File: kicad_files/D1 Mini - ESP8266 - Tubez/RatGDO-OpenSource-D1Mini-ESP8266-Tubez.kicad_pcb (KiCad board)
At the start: 2 copper layers, 51.8 x 65.8 mm, 27 parts, among them J1 Screw_Terminal_01x03, J2 Conn_01x11, J3 Screw_Terminal_01x02, Q1 2N7002, Q2 AO3400A, Q3 AO3400A, Q4 AO3400A, U1 WeMos_D1_mini, U2 K7805-500R3

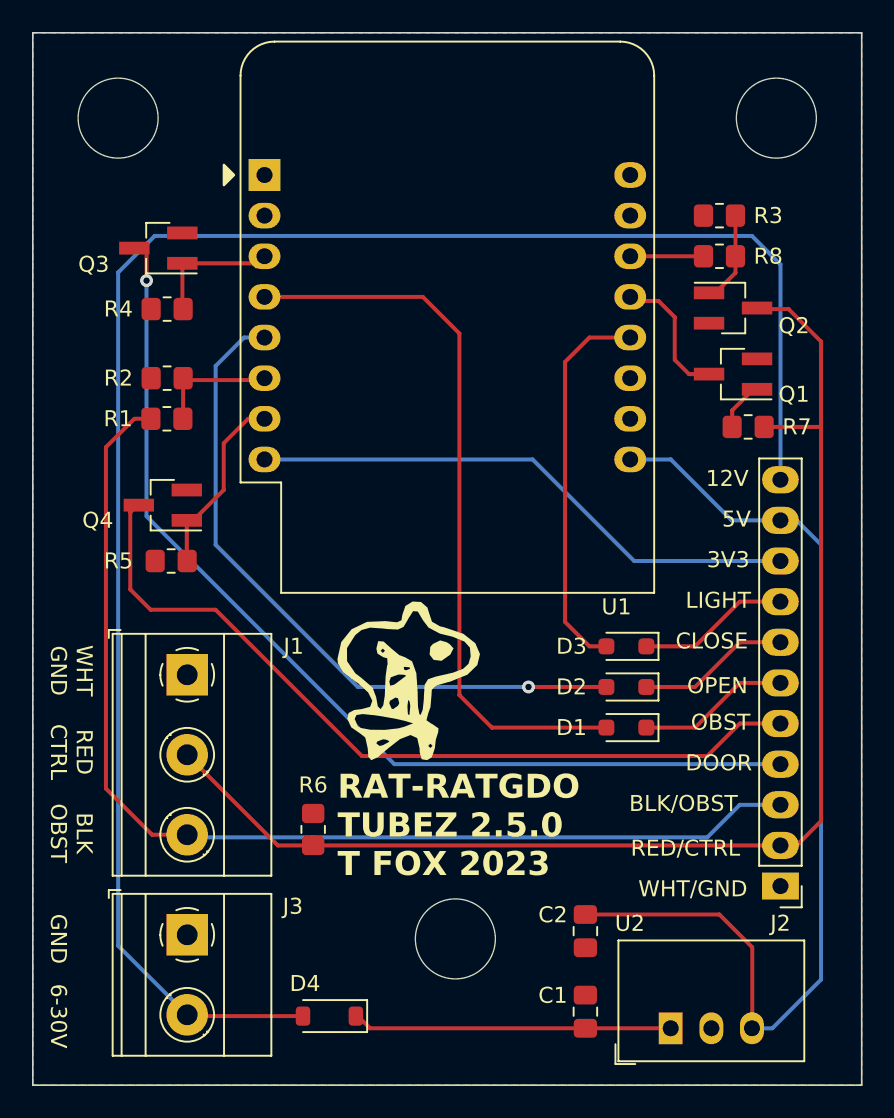
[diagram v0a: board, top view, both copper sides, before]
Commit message: Addition of R7/R6 and R8
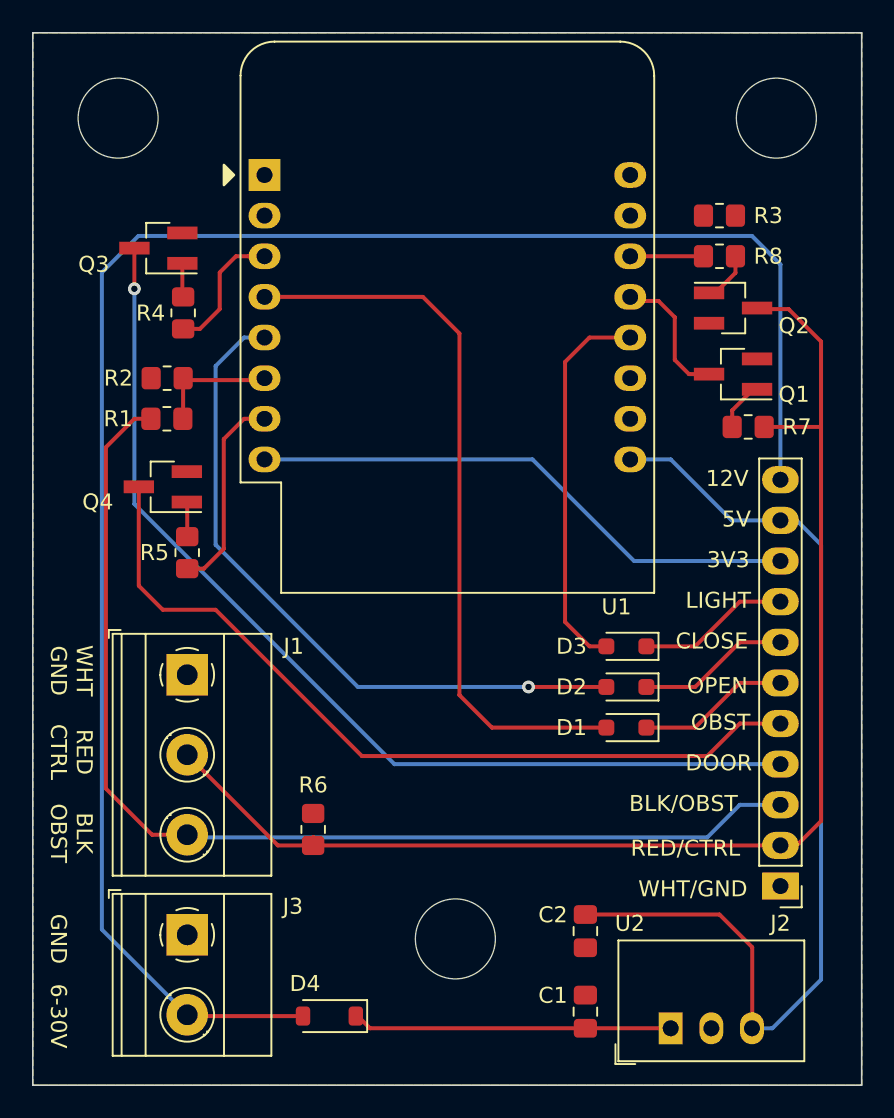
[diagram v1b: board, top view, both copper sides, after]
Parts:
- G***: moved to B.Cu
- moved G*** 3.31 mm to (141.2, 95.8), turned to 180 degrees
- moved Q4 1.15 mm to (123.2, 85.5)
- moved R5 1.13 mm to (124.7, 89.6), turned to 90 degrees
- moved R4 1.03 mm to (124.5, 74.7), turned to 90 degrees
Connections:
- R3 pad 1: Net-(Q2-G) -> /ESP_TX
- R4 pad 1: Net-(Q3-G) -> Net-(U1-D0)
- R4 pad 2: GND -> Net-(Q3-G)
- R5 pad 1: Net-(Q4-G) -> Net-(U1-CS/D8)
- R5 pad 2: GND -> Net-(Q4-G)
- U1 pad 3: Net-(Q3-G) -> Net-(U1-D0)
- U1 pad 7: Net-(Q4-G) -> Net-(U1-CS/D8)
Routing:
- net Net-(U1-CS/D8): track 0.00 -> 12.7 mm
- net Net-(U1-D0): track 0.00 -> 9.33 mm
- net Net-(Q4-G): track 11.3 -> 2.14 mm
- net Net-(Q3-G): track 9.03 -> 2.05 mm
- net Net-(Q2-G): track 5.65 -> 3.13 mm
- net +12V: track 111.6 -> 113.1 mm
- net STS_DOOR: track 62.5 -> 63.1 mm

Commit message: Missed pcb net connection to R3
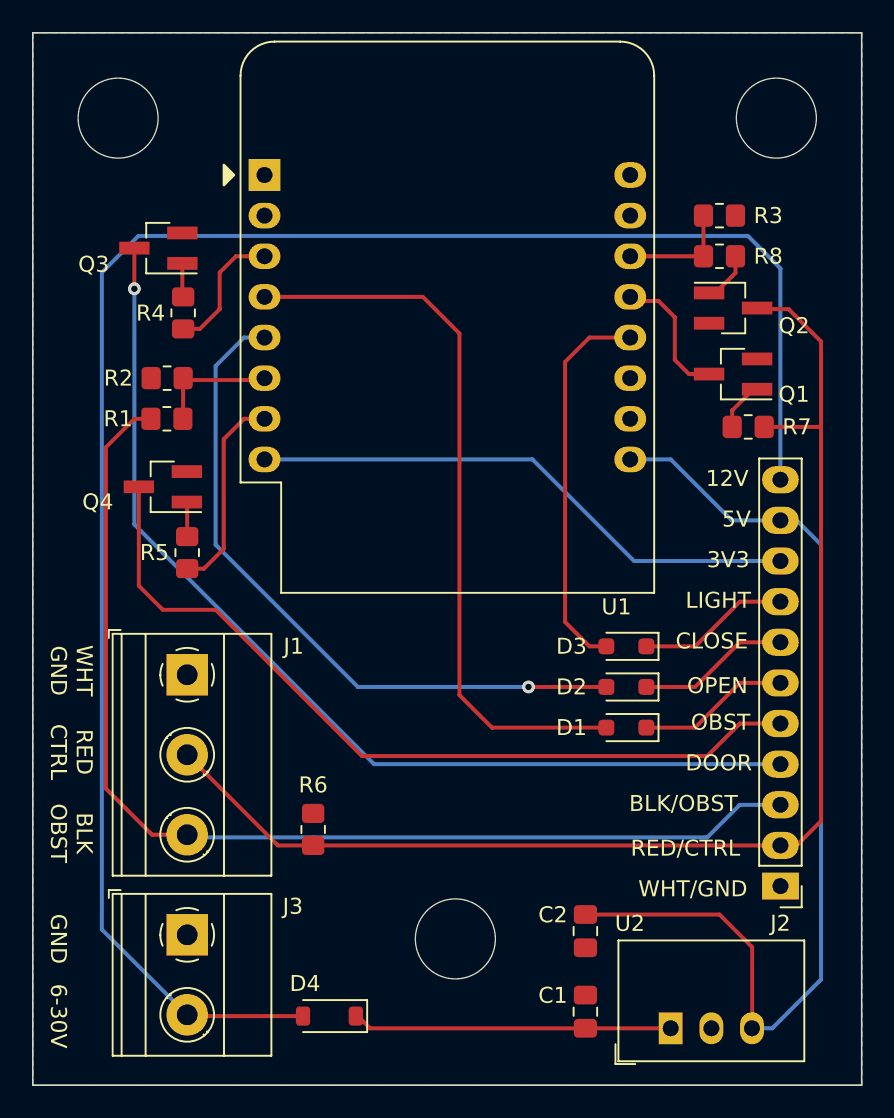
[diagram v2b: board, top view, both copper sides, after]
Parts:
- turned R3 to 0 degrees
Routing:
- net /ESP_TX: track 4.58 -> 7.12 mm
- net STS_DOOR: track 63.1 -> 63.9 mm
